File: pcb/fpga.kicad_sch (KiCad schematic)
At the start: 22 parts

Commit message: Further schematic capture
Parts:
- added U? (x5): 10M02SCE144, Package_QFP:EQFP-144-1EP_20x20mm_P0.5mm_EP4x4mm_ThermalVias, symbol adatv2:10M02SCE144
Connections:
- net ADAT_IN1_USER0: now also U?.87 (IO87); no longer U?.87 (IO87)
- net ADAT_IN1_USER1: now also U?.86 (IO86); no longer U?.86 (IO86)
- net ADAT_IN1_USER2: now also U?.85 (IO85); no longer U?.85 (IO85)
- net ADAT_IN1_USER3: now also U?.84 (IO84); no longer U?.84 (IO84)
- net ADAT_OUT1_USER0: now also U?.77 (IO77); no longer U?.77 (IO77)
- net ADAT_OUT1_USER1: now also U?.76 (IO76); no longer U?.76 (IO76)
- net ADAT_OUT1_USER2: now also U?.75 (IO75); no longer U?.75 (IO75)
- net ADAT_OUT1_USER3: now also U?.74 (IO74); no longer U?.74 (IO74)
- net ADAT_OUT2_USER0: now also U?.100 (IO100); no longer U?.100 (IO100)
- net ADAT_OUT2_USER1: now also U?.99 (IO99); no longer U?.99 (IO99)
- net ADAT_OUT2_USER2: now also U?.98 (IO98); no longer U?.98 (IO98)
- net ADAT_OUT2_USER3: now also U?.97 (IO97); no longer U?.97 (IO97)
- net CLK_44100: now also U?.28 (IO28/CLK1p); no longer U?.28 (IO28/CLK1p)
- net CLK_48000: now also U?.26 (IO26/CLK0p); no longer U?.26 (IO26/CLK0p)
- net DEBUG0: now also U?.3 (IO3); no longer U?.3 (IO3)
- net DEBUG1: now also U?.4 (IO4); no longer U?.4 (IO4)
- net DEBUG2: now also U?.5 (IO5); no longer U?.5 (IO5)
- net DEBUG3: now also U?.6 (IO6); no longer U?.6 (IO6)
- net DEBUG4: now also U?.7 (IO7); no longer U?.7 (IO7)
- net DEBUG5: now also U?.8 (IO8); no longer U?.8 (IO8)
- net DEBUG6: now also U?.9 (IO9); no longer U?.9 (IO9)
- net DEBUG7: now also U?.10 (IO10); no longer U?.10 (IO10)
- net GPIO_F_{s}_SEL: now also U?.24 (IO24); no longer U?.24 (IO24)
- net GPIO_I2S_RESYNC_REQ: now also U?.21 (IO21); no longer U?.21 (IO21)
- net GPIO_I2S_RUNNING: now also U?.62 (IO62); no longer U?.62 (IO62)
- net GPIO_LOOPBACK: now also U?.63 (IO63); no longer U?.63 (IO63)
- net GPIO_MCU_READY: now also U?.67 (IO67); no longer U?.67 (IO67)
- net GPIO_PLL_LOCKED: now also U?.70 (IO70); no longer U?.70 (IO70)
- net I2S_CH1-8_BCLK: now also U?.46 (IO46); no longer U?.46 (IO46)
- net I2S_CH1-8_LRCLK: now also U?.49 (IO49); no longer U?.49 (IO49)
- net I2S_CH1-8_MISO: now also U?.47 (IO47); no longer U?.47 (IO47)
- net I2S_CH1-8_MOSI: now also U?.48 (IO48); no longer U?.48 (IO48)
- net I2S_CH9-16_BCLK: now also U?.51 (IO51); no longer U?.51 (IO51)
- net I2S_CH9-16_LRCLK: now also U?.54 (IO54); no longer U?.54 (IO54)
- net I2S_CH9-16_MISO: now also U?.52 (IO52); no longer U?.52 (IO52)
- net I2S_CH9-16_MOSI: now also U?.53 (IO53); no longer U?.53 (IO53)
- net I2S_MCLK: now also U?.40 (IO40); no longer U?.40 (IO40)
- net WORD_CLK: now also U?.41 (IO41); no longer U?.41 (IO41)

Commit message: Assign most of the footprints to schematic components
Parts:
- C145, C146, C147, C148: renamed from C?; footprint (none) -> Capacitor_SMD:C_0805_2012Metric_Pad1.18x1.45mm_HandSolder
- R121: renamed from R?; footprint (none) -> Resistor_SMD:R_0805_2012Metric_Pad1.20x1.40mm_HandSolder
- TP110, TP111, TP112, TP113, TP114, TP115, TP116, TP117: renamed from TP?; footprint (none) -> TestPoint:TestPoint_Pad_D2.5mm; now left out of the parts list
- Y103: renamed from Y?; footprint Oscillator:Oscillator_SMD_Fordahl_DFAS15-4Pin_5.0x3.2mm -> Oscillator:Oscillator_SMD_Abracon_ASE-4Pin_3.2x2.5mm_HandSoldering
- gave numbers to parts that had none: 3
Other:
- note added: "FPGA IO pins"
- note added: "FPGA clock input"
- note added: "Unused inverters"
- moved on the sheet: U101D, U101H, U102C, U102D, U102E, U102F

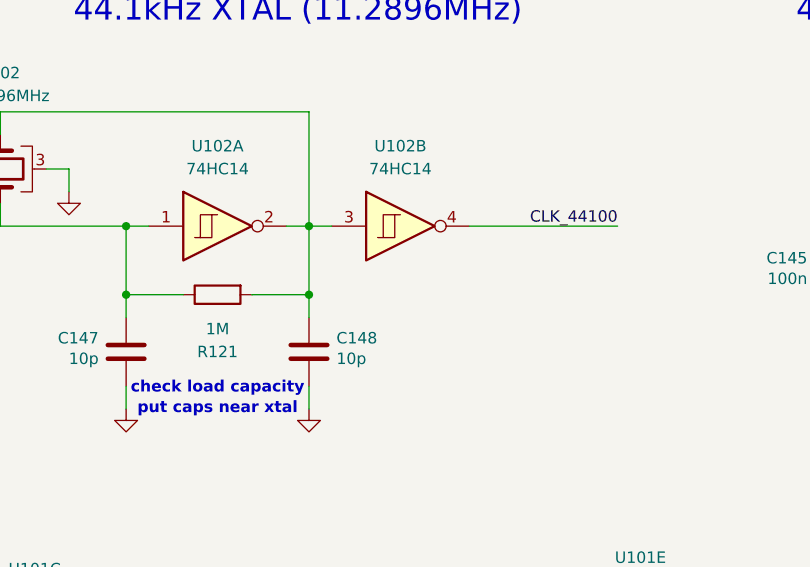
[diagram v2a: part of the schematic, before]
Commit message: Finish assigning footprints to project
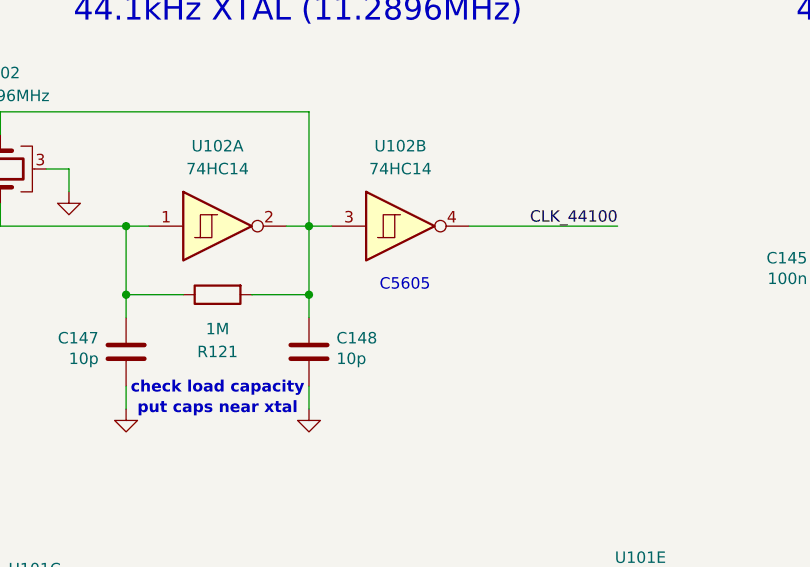
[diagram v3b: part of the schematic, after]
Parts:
- U102: footprint (none) -> Package_SO:SOIC-14_3.9x8.7mm_P1.27mm
- Y102: footprint (none) -> Oscillator:Oscillator_SMD_Abracon_ASE-4Pin_3.2x2.5mm_HandSoldering
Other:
- note added: "C5605"
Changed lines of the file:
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@@
 		)
 	)
+	(text "C5605"
+		(exclude_from_sim no)
+		(at 84.328 51.054 0)
+		(effects
+			(font
+				(size 1.27 1.27)
+			)
+		)
+	)
 	(text "Unused inverters"
 		(exclude_from_sim no)
@@
 			)
 		)
-		(property "Footprint" ""
+		(property "Footprint" "Package_SO:SOIC-14_3.9x8.7mm_P1.27mm"
 			(at 241.3 153.67 0)
 			(effects
@@
 			)
 		)
-		(property "Footprint" ""
+		(property "Footprint" "Package_SO:SOIC-14_3.9x8.7mm_P1.27mm"
 			(at 264.16 153.67 0)
 			(effects
@@
 			)
 		)
-		(property "Footprint" ""
+		(property "Footprint" "Package_SO:SOIC-14_3.9x8.7mm_P1.27mm"
 			(at 218.44 153.67 0)
 			(effects
@@
 			)
 		)
-		(property "Footprint" ""
+		(property "Footprint" "Package_SO:SOIC-14_3.9x8.7mm_P1.27mm"
 			(at 63.5 44.45 0)
 			(effects
@@
 			)
 		)
-		(property "Footprint" ""
+		(property "Footprint" "Oscillator:Oscillator_SMD_Abracon_ASE-4Pin_3.2x2.5mm_HandSoldering"
 			(at 39.37 38.1 0)
 			(effects
@@
 			)
 		)
-		(property "Footprint" ""
+		(property "Footprint" "Package_SO:SOIC-14_3.9x8.7mm_P1.27mm"
 			(at 83.82 44.45 0)
 			(effects
@@
 			)
 		)
-		(property "Footprint" ""
+		(property "Footprint" "Package_SO:SOIC-14_3.9x8.7mm_P1.27mm"
 			(at 194.31 153.67 0)
 			(effects

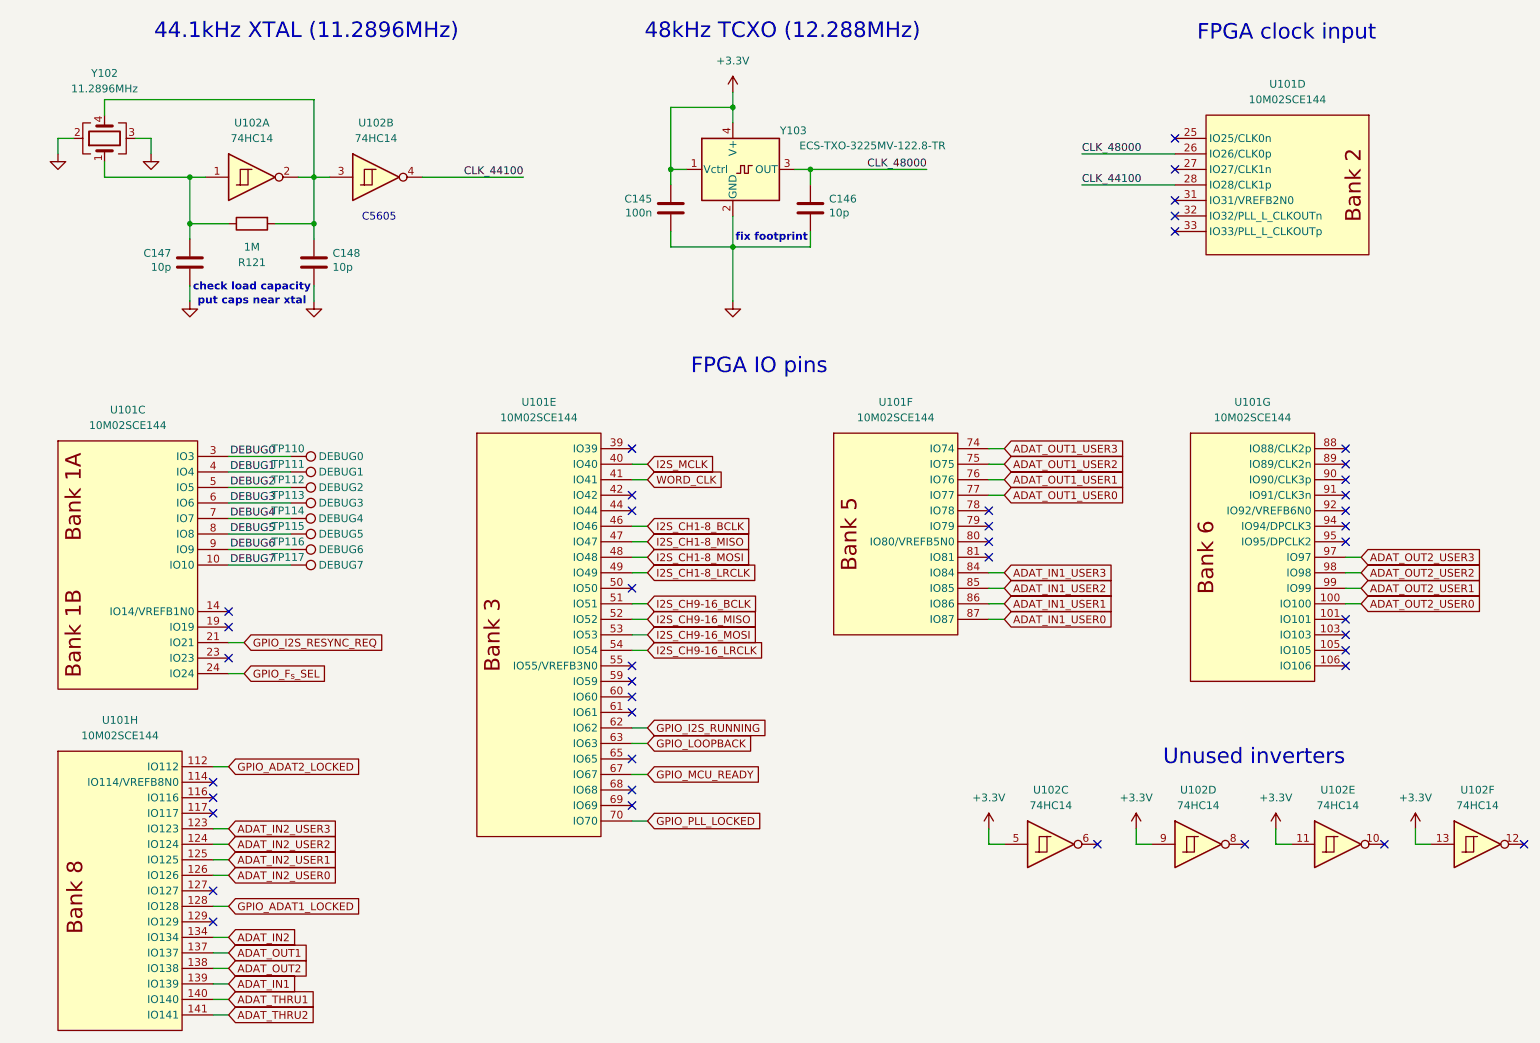
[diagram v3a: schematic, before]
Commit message: Finish drawing IO/Supply board
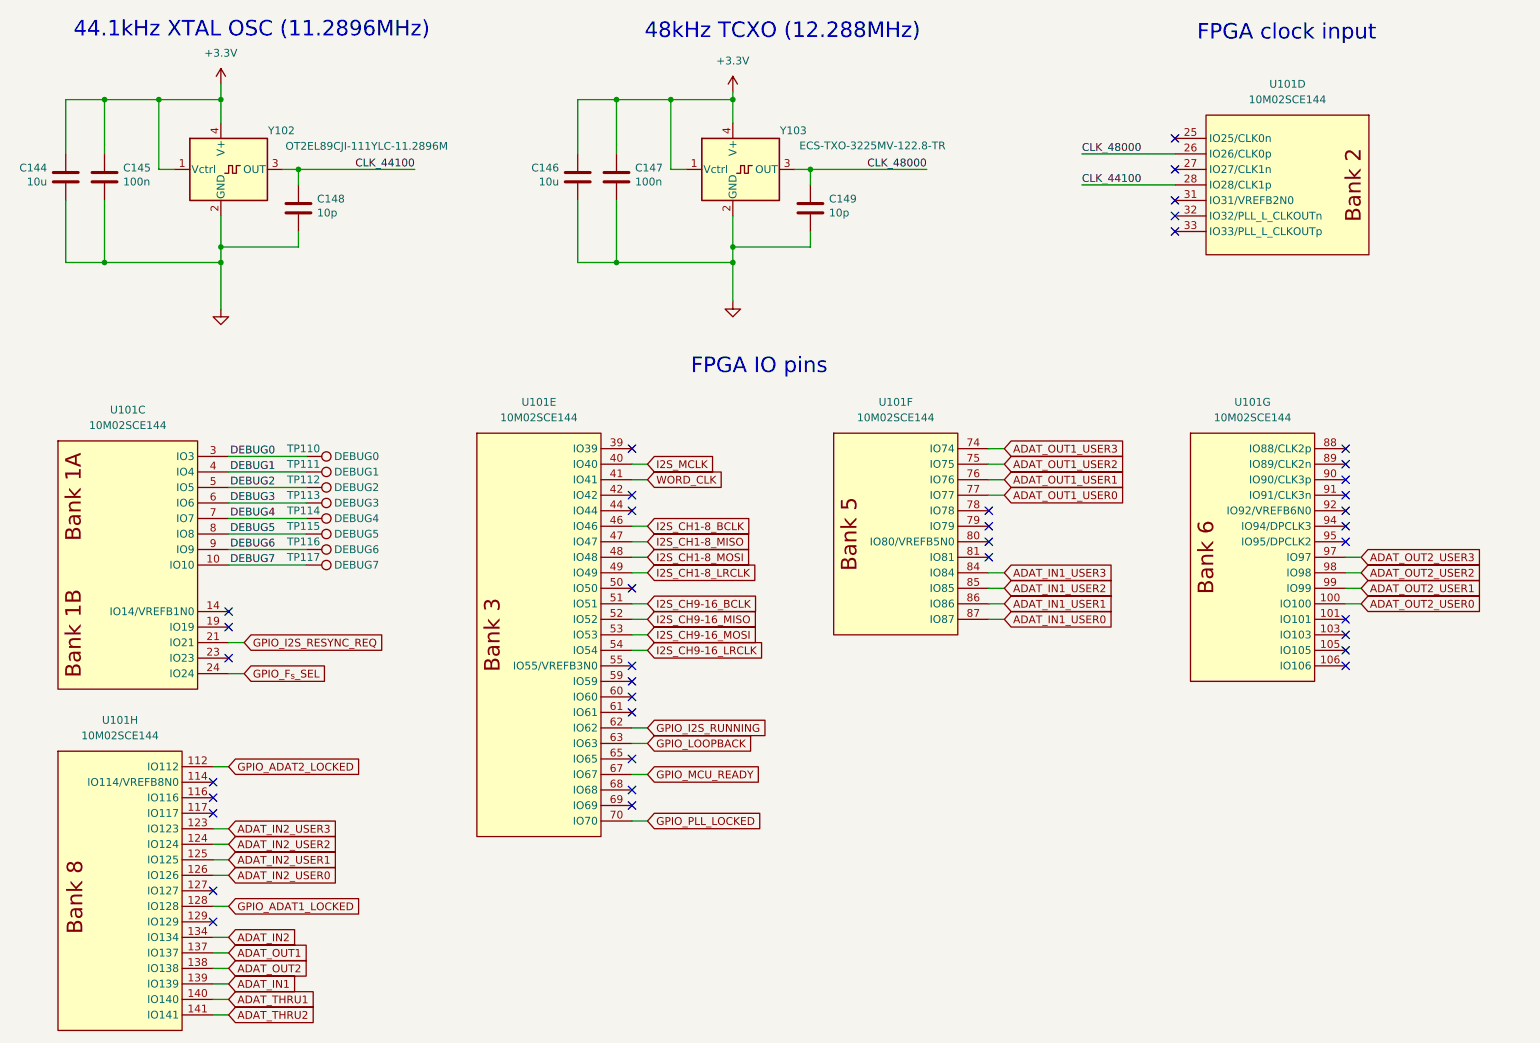
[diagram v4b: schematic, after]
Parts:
- removed R121: 1M, Resistor_SMD:R_0805_2012Metric_Pad1.20x1.40mm_HandSolder, symbol Device:R
- removed U102: 74HC14, Package_SO:SOIC-14_3.9x8.7mm_P1.27mm, symbol 74xx:74HC14
- removed Y102: 11.2896MHz, Oscillator:Oscillator_SMD_Abracon_ASE-4Pin_3.2x2.5mm_HandSoldering, symbol Device:Crystal_GND23
- added C144, C146: 10u, Capacitor_SMD:C_1206_3216Metric_Pad1.33x1.80mm_HandSolder, symbol Device:C
- added Y102: OT2EL89CJI-111YLC-11.2896M, Oscillator:Oscillator_SMD_Abracon_ASE-4Pin_3.2x2.5mm_HandSoldering, symbol Oscillator:DFA-S15
- C147: value 10p -> 100n
- renumbered C146 to C149
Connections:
- net +3.3V: now also C147.1, C144.1, C146.1, Y102.1 (Vctrl), Y102.4 (V+)
- net CLK_44100: now also C148.1, Y102.3 (OUT)
- net GND: now also C144.2, C146.2, Y102.2 (GND)
- no-connect marks 43 -> 39
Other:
- note added: "44.1kHz XTAL OSC (11.2896MHz)"
- note removed: "44.1kHz XTAL (11.2896MHz)"
- note removed: "C5605"
- note removed: "Unused inverters"
- note removed: "check load capacity"
- note removed: "fix footprint"
- note removed: "put caps near xtal"
- moved on the sheet: TP110, TP111, TP112, TP113, TP114, TP115, TP116, TP117

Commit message: Add missing CAD models of I/O electronic components
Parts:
- U101: footprint Package_QFP:EQFP-144-1EP_20x20mm_P0.5mm_EP4x4mm_ThermalVias -> adatv2:EQFP-144-1EP_20x20mm_P0.5mm_EP4x4mm
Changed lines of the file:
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@@
 			)
 		)
-		(property "Footprint" "Package_QFP:EQFP-144-1EP_20x20mm_P0.5mm_EP4x4mm_ThermalVias"
+		(property "Footprint" "adatv2:EQFP-144-1EP_20x20mm_P0.5mm_EP4x4mm"
 			(at 42.418 109.728 0)
 			(effects
@@
 			)
 		)
-		(property "Footprint" "Package_QFP:EQFP-144-1EP_20x20mm_P0.5mm_EP4x4mm_ThermalVias"
+		(property "Footprint" "adatv2:EQFP-144-1EP_20x20mm_P0.5mm_EP4x4mm"
 			(at 169.418 51.308 0)
 			(effects
@@
 			)
 		)
-		(property "Footprint" "Package_QFP:EQFP-144-1EP_20x20mm_P0.5mm_EP4x4mm_ThermalVias"
+		(property "Footprint" "adatv2:EQFP-144-1EP_20x20mm_P0.5mm_EP4x4mm"
 			(at 43.688 56.388 0)
 			(effects
@@
 			)
 		)
-		(property "Footprint" "Package_QFP:EQFP-144-1EP_20x20mm_P0.5mm_EP4x4mm_ThermalVias"
+		(property "Footprint" "adatv2:EQFP-144-1EP_20x20mm_P0.5mm_EP4x4mm"
 			(at 231.902 -5.842 0)
 			(effects
@@
 			)
 		)
-		(property "Footprint" "Package_QFP:EQFP-144-1EP_20x20mm_P0.5mm_EP4x4mm_ThermalVias"
+		(property "Footprint" "adatv2:EQFP-144-1EP_20x20mm_P0.5mm_EP4x4mm"
 			(at 114.808 67.818 0)
 			(effects
@@
 			)
 		)
-		(property "Footprint" "Package_QFP:EQFP-144-1EP_20x20mm_P0.5mm_EP4x4mm_ThermalVias"
+		(property "Footprint" "adatv2:EQFP-144-1EP_20x20mm_P0.5mm_EP4x4mm"
 			(at 227.838 55.118 0)
 			(effects

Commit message: Finish first revision of main pcb
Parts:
- added TP118, TP119, TP120, TP121, TP122, TP123: ${NET_NAME(1)}, TestPoint:TestPoint_Pad_D2.5mm, symbol Connector:TestPoint
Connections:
- net ADAT_IN1: now also TP121.1
- net ADAT_IN1_USER0: now also U101.112 (IO112); no longer U101.87 (IO87)
- net ADAT_IN1_USER1: now also U101.116 (IO116); no longer U101.86 (IO86)
- net ADAT_IN1_USER2: now also U101.117 (IO117); no longer U101.85 (IO85)
- net ADAT_IN1_USER3: now also U101.24 (IO24); no longer U101.84 (IO84)
- net ADAT_IN2: now also TP118.1
- net ADAT_IN2_USER1: now also U101.127 (IO127); no longer U101.125 (IO125)
- net ADAT_IN2_USER2: now also U101.128 (IO128); no longer U101.124 (IO124)
- net ADAT_IN2_USER3: now also U101.129 (IO129); no longer U101.123 (IO123)
- net ADAT_OUT1: now also TP119.1
- net ADAT_OUT1_USER0: now also U101.14 (IO14/VREFB1N0); no longer U101.77 (IO77)
- net ADAT_OUT1_USER1: now also U101.19 (IO19); no longer U101.76 (IO76)
- net ADAT_OUT1_USER2: now also U101.21 (IO21); no longer U101.75 (IO75)
- net ADAT_OUT1_USER3: now also U101.23 (IO23); no longer U101.74 (IO74)
- net ADAT_OUT2: now also TP120.1
- net ADAT_THRU1: now also TP122.1
- net ADAT_THRU2: now also TP123.1
- net GPIO_ADAT1_LOCKED: now also U101.84 (IO84); no longer U101.128 (IO128)
- net GPIO_ADAT2_LOCKED: now also U101.85 (IO85); no longer U101.112 (IO112)
- net GPIO_F_{s}_SEL: now also U101.75 (IO75); no longer U101.24 (IO24)
- net GPIO_I2S_RESYNC_REQ: now also U101.74 (IO74); no longer U101.21 (IO21)
- net I2S_CH1-8_BCLK: now also U101.95 (IO95/DPCLK2); no longer U101.46 (IO46)
- net I2S_CH1-8_LRCLK: now also U101.88 (IO88/CLK2p); no longer U101.49 (IO49)
- net I2S_CH1-8_MISO: now also U101.125 (IO125); no longer U101.47 (IO47)
- net I2S_CH1-8_MOSI: now also U101.124 (IO124); no longer U101.48 (IO48)
- net I2S_CH9-16_BCLK: now also U101.106 (IO106); no longer U101.51 (IO51)
- net I2S_CH9-16_LRCLK: now also U101.123 (IO123); no longer U101.54 (IO54)
- net I2S_CH9-16_MISO: now also U101.105 (IO105); no longer U101.52 (IO52)
- net I2S_CH9-16_MOSI: now also U101.103 (IO103); no longer U101.53 (IO53)
- no-connect marks 39 -> 37

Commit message: Add PCB production files
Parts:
- TP110, TP111, TP112, TP113, TP114, TP115, TP116, TP117, TP118, TP119, TP120, TP121, TP122, TP123: footprint TestPoint:TestPoint_Pad_D2.5mm -> TestPoint:TestPoint_Pad_D1.5mm
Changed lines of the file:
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@@
 			)
 		)
-		(property "Footprint" "TestPoint:TestPoint_Pad_D2.5mm"
+		(property "Footprint" "TestPoint:TestPoint_Pad_D1.5mm"
 			(at 72.39 110.49 0)
 			(effects
@@
 			)
 		)
-		(property "Footprint" "TestPoint:TestPoint_Pad_D2.5mm"
+		(property "Footprint" "TestPoint:TestPoint_Pad_D1.5mm"
 			(at 72.39 102.87 0)
 			(effects
@@
 			)
 		)
-		(property "Footprint" "TestPoint:TestPoint_Pad_D2.5mm"
+		(property "Footprint" "TestPoint:TestPoint_Pad_D1.5mm"
 			(at 72.39 95.25 0)
 			(effects
@@
 			)
 		)
-		(property "Footprint" "TestPoint:TestPoint_Pad_D2.5mm"
+		(property "Footprint" "TestPoint:TestPoint_Pad_D1.5mm"
 			(at 72.39 107.95 0)
 			(effects
@@
 			)
 		)
-		(property "Footprint" "TestPoint:TestPoint_Pad_D2.5mm"
+		(property "Footprint" "TestPoint:TestPoint_Pad_D1.5mm"
 			(at 72.39 105.41 0)
 			(effects
@@
 			)
 		)
-		(property "Footprint" "TestPoint:TestPoint_Pad_D2.5mm"
+		(property "Footprint" "TestPoint:TestPoint_Pad_D1.5mm"
 			(at 72.39 100.33 0)
 			(effects
@@
 			)
 		)
-		(property "Footprint" "TestPoint:TestPoint_Pad_D2.5mm"
+		(property "Footprint" "TestPoint:TestPoint_Pad_D1.5mm"
 			(at 114.3 186.69 0)
 			(effects
@@
 			)
 		)
-		(property "Footprint" "TestPoint:TestPoint_Pad_D2.5mm"
+		(property "Footprint" "TestPoint:TestPoint_Pad_D1.5mm"
 			(at 114.3 173.99 0)
 			(effects
@@
 			)
 		)
-		(property "Footprint" "TestPoint:TestPoint_Pad_D2.5mm"
+		(property "Footprint" "TestPoint:TestPoint_Pad_D1.5mm"
 			(at 114.3 181.61 0)
 			(effects
@@
 			)
 		)
-		(property "Footprint" "TestPoint:TestPoint_Pad_D2.5mm"
+		(property "Footprint" "TestPoint:TestPoint_Pad_D1.5mm"
 			(at 114.3 184.15 0)
 			(effects
@@
 			)
 		)
-		(property "Footprint" "TestPoint:TestPoint_Pad_D2.5mm"
+		(property "Footprint" "TestPoint:TestPoint_Pad_D1.5mm"
 			(at 72.39 113.03 0)
 			(effects
@@
 			)
 		)
-		(property "Footprint" "TestPoint:TestPoint_Pad_D2.5mm"
+		(property "Footprint" "TestPoint:TestPoint_Pad_D1.5mm"
 			(at 72.39 97.79 0)
 			(effects
@@
 			)
 		)
-		(property "Footprint" "TestPoint:TestPoint_Pad_D2.5mm"
+		(property "Footprint" "TestPoint:TestPoint_Pad_D1.5mm"
 			(at 114.3 179.07 0)
 			(effects
@@
 			)
 		)
-		(property "Footprint" "TestPoint:TestPoint_Pad_D2.5mm"
+		(property "Footprint" "TestPoint:TestPoint_Pad_D1.5mm"
 			(at 114.3 176.53 0)
 			(effects
